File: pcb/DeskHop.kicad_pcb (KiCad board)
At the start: 2 copper layers, 66.9 x 74.5 mm, 12 parts, among them J1 Keyboard In, J2 Debug2, J3 Debug1, J4 Mouse In, U1 Pico Primary, U2 Pico Secondary, U4 ADuM1201BR

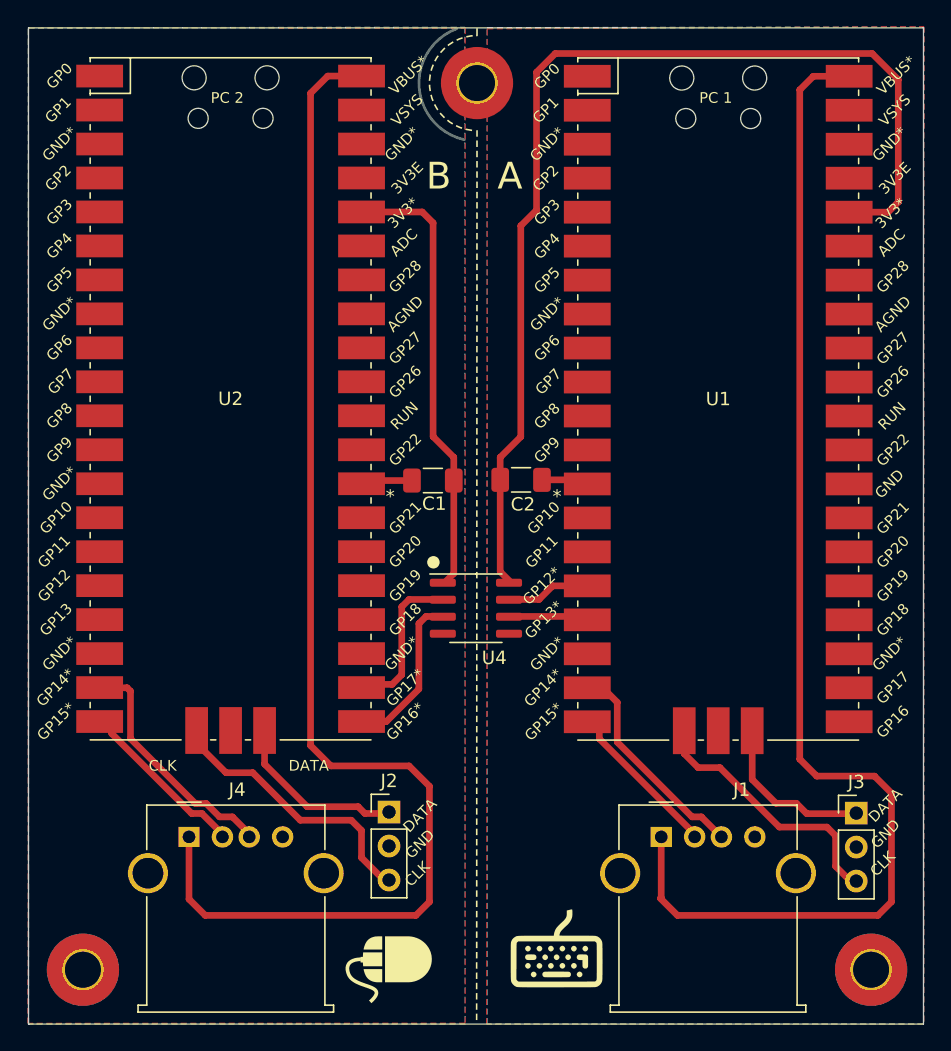
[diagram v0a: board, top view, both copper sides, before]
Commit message: Changed design to Type C pico copy
Modifications done to adapt design to Type C version of Pico-copy available in India. Detail changes in PCB Schematics.
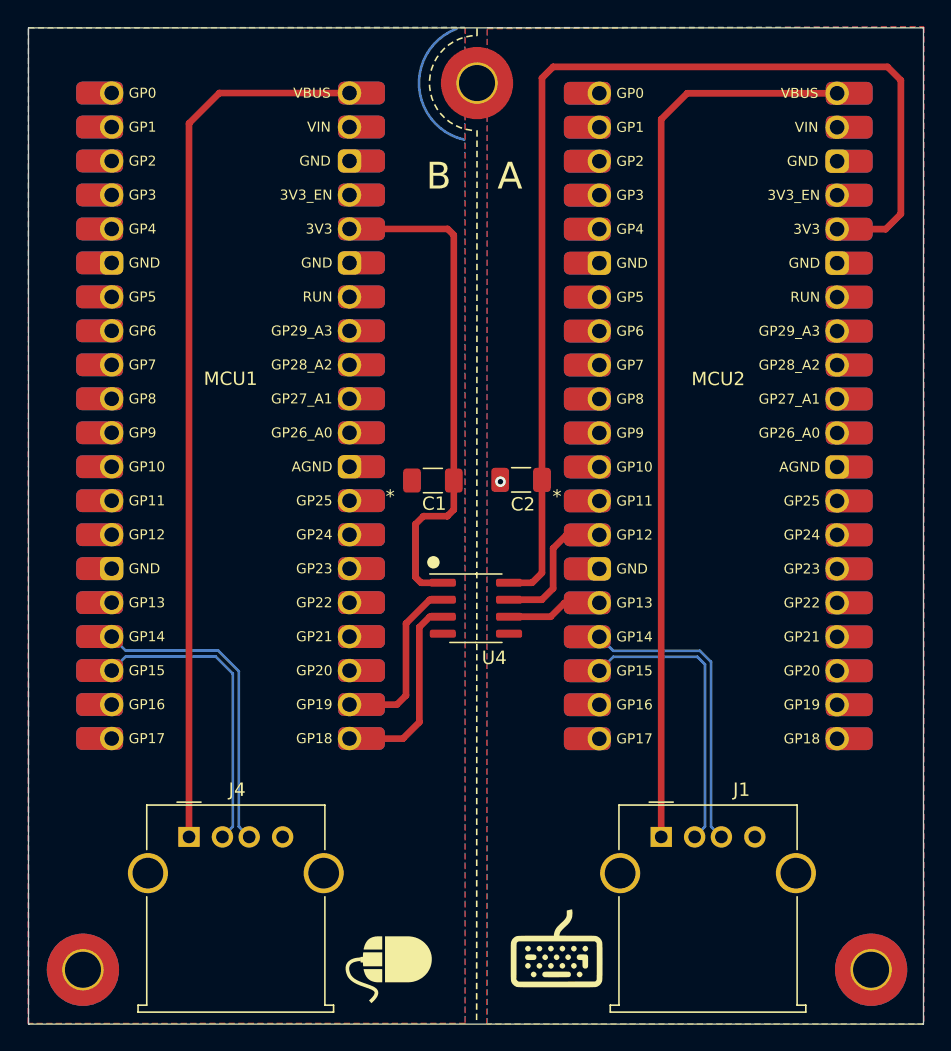
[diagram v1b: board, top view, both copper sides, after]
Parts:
- removed J2: Debug2, Connector_PinHeader_2.54mm:PinHeader_1x03_P2.54mm_Vertical
- removed J3: Debug1, Connector_PinHeader_2.54mm:PinHeader_1x03_P2.54mm_Vertical
- removed U1: Pico Primary, MCU_RaspberryPi_and_Boards:RPi_Pico_SMD_Nohole
- removed U2: Pico Secondary, MCU_RaspberryPi_and_Boards:RPi_Pico_SMD_Nohole
- added MCU1: ~, OEM_like:Pico_like, F.Cu at (48.9, 68.8)
- added MCU2: ~, OEM_like:Pico_like, F.Cu at (85.3, 68.8)
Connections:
- net Net-(U2-3V3) renamed 3V3_BUS2
- C2 pad 1: Net-(U1-3V3) -> GND2
- C2 pad 2: GND2 -> 3V3_BUS1
- H3 pad 1: GND2 -> unconnected-(H3-Pad1)
- J1 pad 1: Net-(J1-VBUS) -> VBUS1
- J1 pad 2: Net-(J1-D-) -> MCU2 D-
- J1 pad 3: Net-(J1-D+) -> MCU2 D+
- J4 pad 1: Net-(J4-VBUS) -> VBUS2
- J4 pad 2: Net-(J4-D-) -> MCU1 D-
- J4 pad 3: Net-(J4-D+) -> MCU1 D+
- U4 pad 2: /UART B RX -> UART B RX
- U4 pad 3: /UART B TX -> UART B TX
- U4 pad 6: (no net) -> UART A RX
- U4 pad 7: /UART A TX -> UART A TX
- U4 pad 8: Net-(U1-3V3) -> 3V3_BUS1
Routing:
- net Net-(J4-VBUS): track 94.6 -> 0.00 mm
- net Net-(J1-VBUS): track 91.9 -> 0.00 mm
- net 3V3_BUS1: track 0.00 -> 82.6 mm
- net Net-(U1-3V3): track 82.1 -> 0.00 mm
- net VBUS1: track 0.00 -> 67.6 mm
- net VBUS2: track 0.00 -> 66.3 mm
- net MCU1 D+: track 0.00 -> 23.3 mm
- net MCU1 D-: track 0.00 -> 22.5 mm
- net MCU2 D+: track 0.00 -> 22.5 mm
- net MCU2 D-: track 0.00 -> 21.8 mm
- net Net-(J2-Pin_3): track 21.4 -> 0.00 mm
- net Net-(J3-Pin_3): track 19.6 -> 0.00 mm
- net Net-(J4-D+): track 15.7 -> 0.00 mm
- net Net-(J1-D+): track 15.6 -> 0.00 mm
- net UART B TX: track 0.00 -> 14.9 mm
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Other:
- board text added: "locked"
- board text removed: "CLK"
- board text removed: "DATA"
- board text removed: "DeskHop - Keyboard/Mouse Switch by Hrvoje Cavrak, 12/2023 https://github.com/hrvach"
- board text removed: "GND"
- board text removed: "PC 1"
- board text removed: "PC 2"

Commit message: reverted back to orignal GPIO for MCU 1
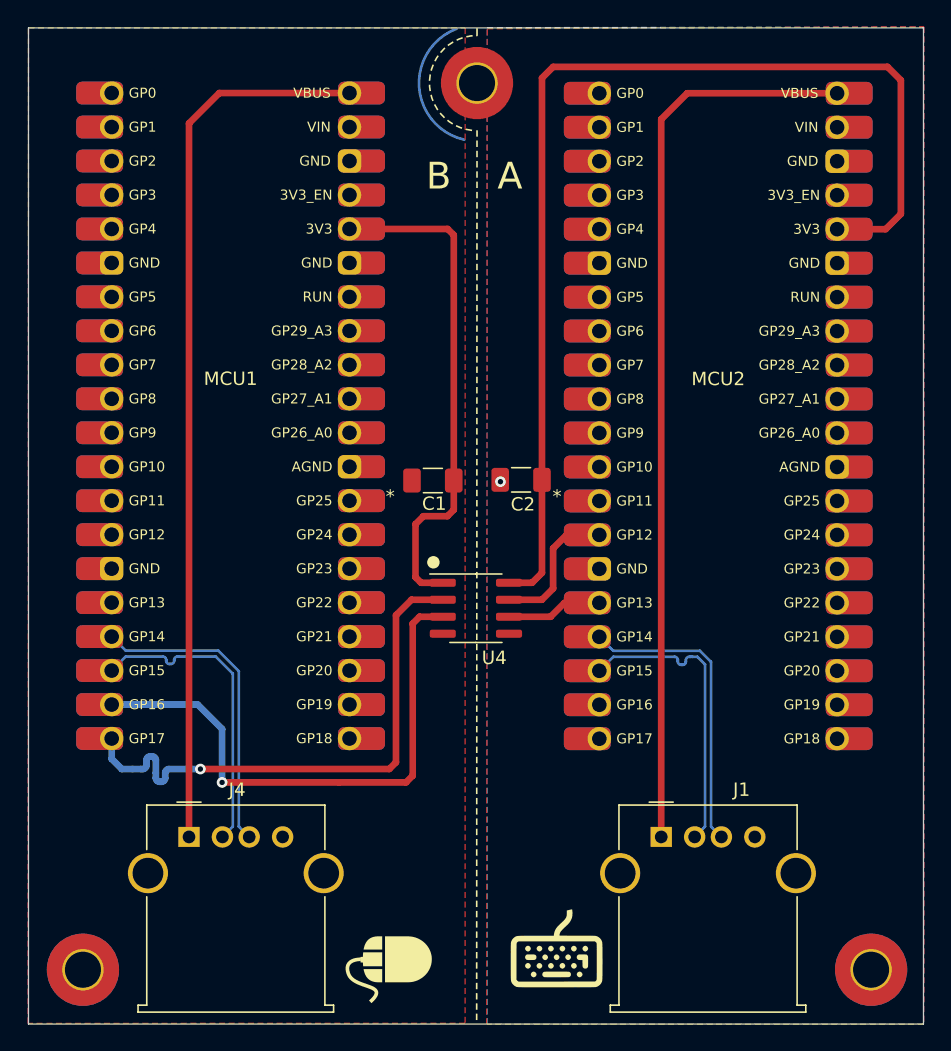
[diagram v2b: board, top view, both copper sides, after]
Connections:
- MCU1 pad 19: unconnected-(MCU1-GP16-Pad19) -> UART B TX
- MCU1 pad 20: unconnected-(MCU1-GP17-Pad20) -> UART B RX
- MCU1 pad 21: UART B TX -> unconnected-(MCU1-GP18-Pad21)
- MCU1 pad 22: UART B RX -> unconnected-(MCU1-GP19-Pad22)_0
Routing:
- net UART B RX: track 13.4 -> 41.3 mm, vias 0 -> 1
- net UART B TX: track 14.9 -> 41.3 mm, vias 0 -> 1
- net MCU2 D-: track 21.8 -> 22.5 mm
- net MCU1 D-: track 22.5 -> 23.2 mm
- removed copper zone on B.Cu, net GND
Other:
- board text added: "DeskHop_Type-C - Keyboard/Mouse Switch by Hrvoje Cavrak, 12/2023 (https://github.com/hrvach) Modified by ~ Umgbhalla & strek https://github.com/umgbhalla/deskhop-type-c"
- board text removed: "locked"
